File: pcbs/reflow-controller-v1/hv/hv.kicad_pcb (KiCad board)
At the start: 2 copper layers, 53 parts, among them J101 EB163A-03-C-180, J102 EB163A-02-C-180, J103 EB163A-02-C-180, J104 EB163A-02-C-180, J105 EB163A-02-C-180, J801 Power, J802 Data, Q701 MMBT3904, Q702 140357145200, U301 MOC3043SM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

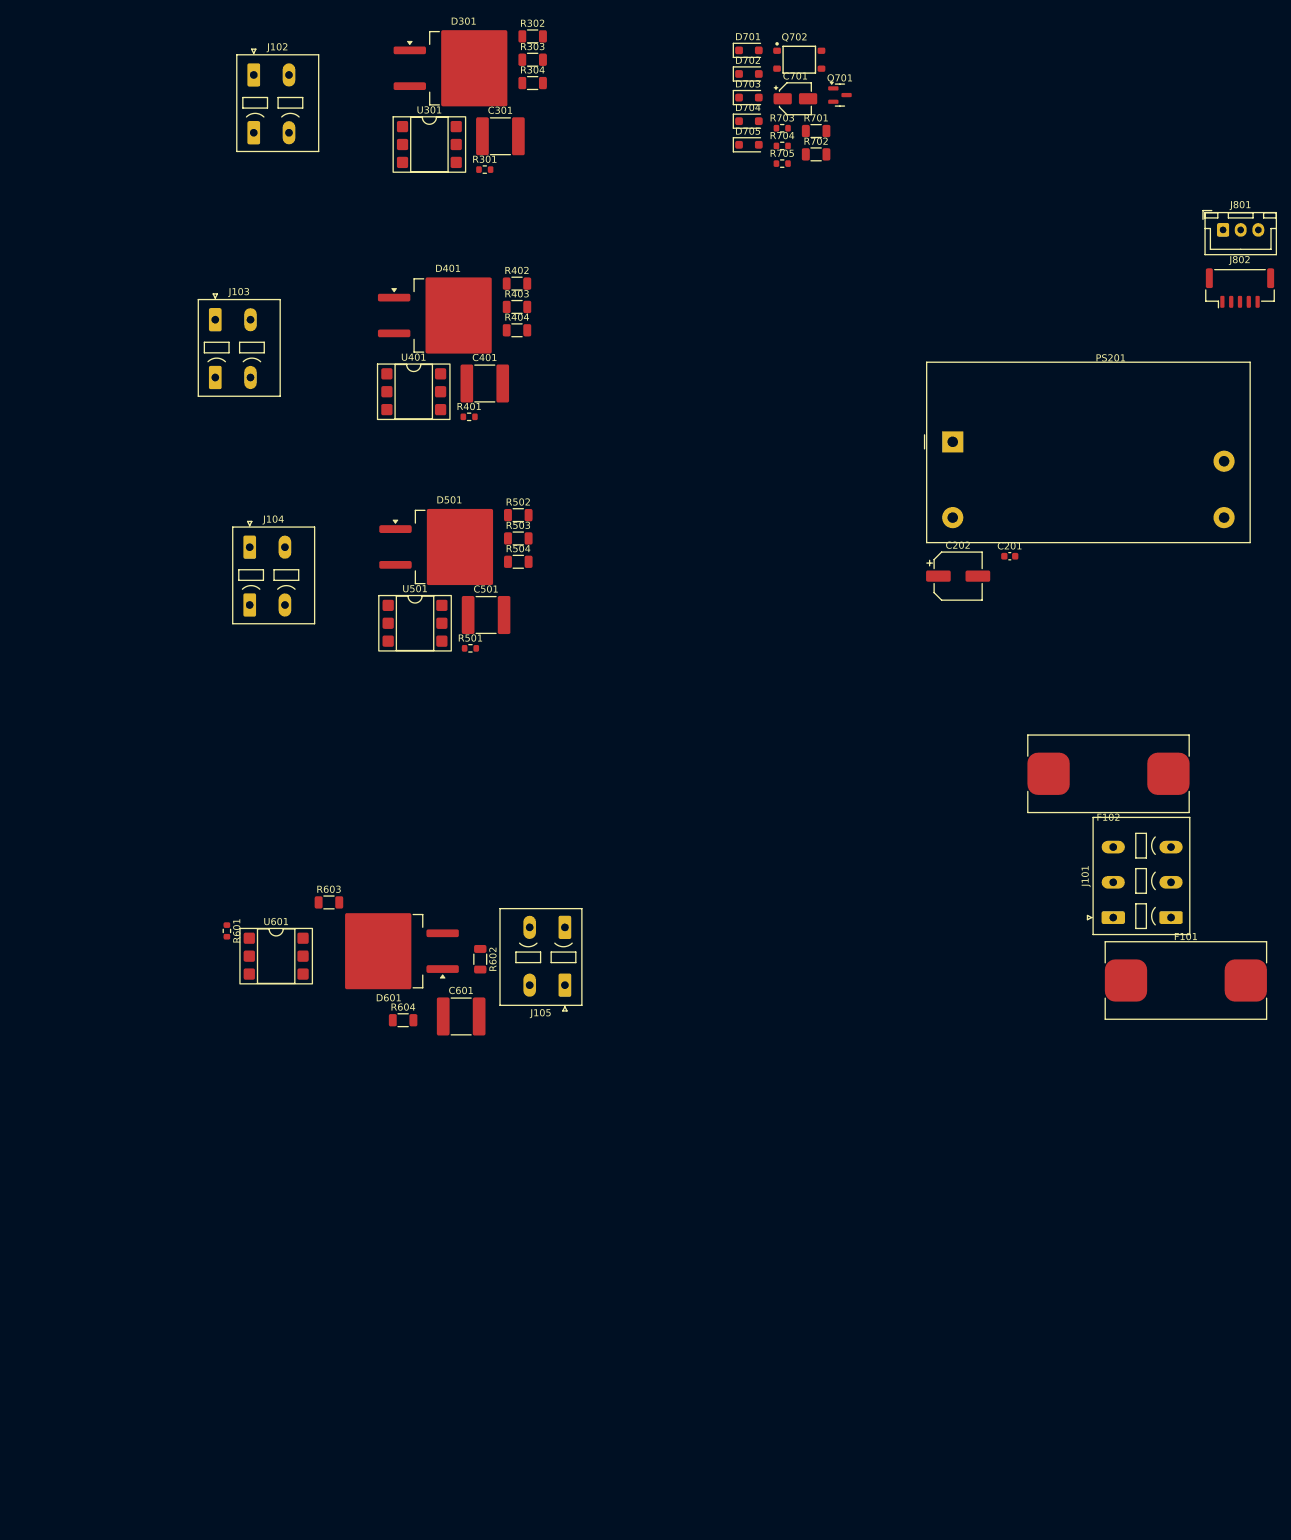
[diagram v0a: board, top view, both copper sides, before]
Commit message: Initial hv placing
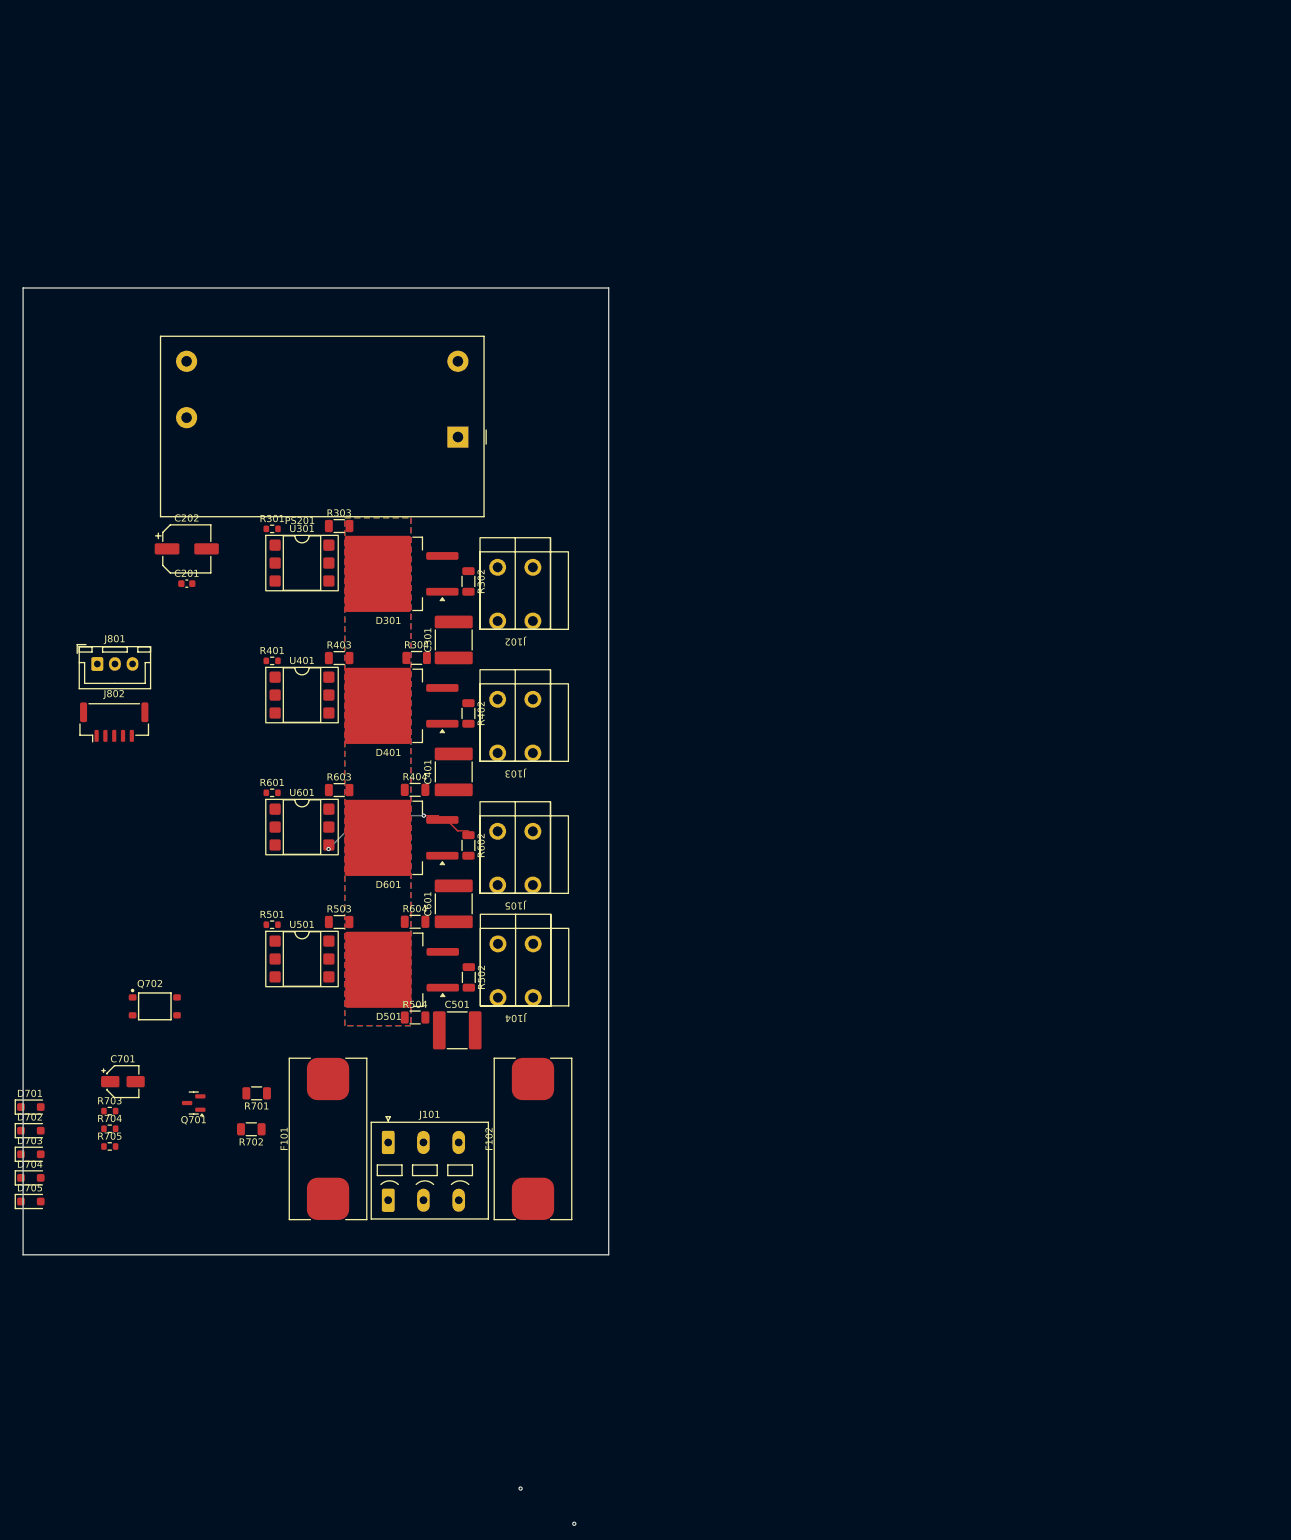
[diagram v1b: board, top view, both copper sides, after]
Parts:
- J102, J103, J104, J105: value EB163A-02-C-180 -> 691401700002B; footprint Connector_Phoenix_SPT:PhoenixContact_SPT_2.5_2-V-5.0-EX_1x02_P5.0mm_Vertical -> wuerth:691401700002B
- moved D701 181.3 mm to (41.5, 172.2)
- moved D702 181.3 mm to (41.5, 175.6)
- moved D703 181.3 mm to (41.5, 178.9)
- moved D704 181.3 mm to (41.5, 182.3)
- moved D705 181.3 mm to (41.5, 185.6)
- moved J801 171.2 mm to (51.0, 109.3)
- moved J802 171.2 mm to (53.4, 117.6)
- moved Q701 169.9 mm to (64.7, 171.7), turned to 180 degrees
- moved C701 169.0 mm to (54.6, 168.6)
- moved R703 169.0 mm to (52.7, 172.8)
- moved R704 169.0 mm to (52.7, 175.3)
- moved R705 169.0 mm to (52.7, 177.8)
- moved Q702 162.5 mm to (59.1, 157.9)
- moved R702 159.9 mm to (72.8, 175.4), turned to 180 degrees
- moved R701 157.9 mm to (73.6, 170.3), turned to 180 degrees
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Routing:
- net Net-(D601-G): track 0.00 -> 23.9 mm, vias 0 -> 2
- net (no net): vias 0 -> 2
- added copper zone on B.Cu, net /Phase_L
- added copper zone on F.Cu, net /Phase_L
- added copper zone on In1.Cu, net /Phase_L
- added copper zone on In2.Cu, net /Phase_L
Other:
- board outline added: 83.1 x 137.2 mm
- copper layers 2 -> 4

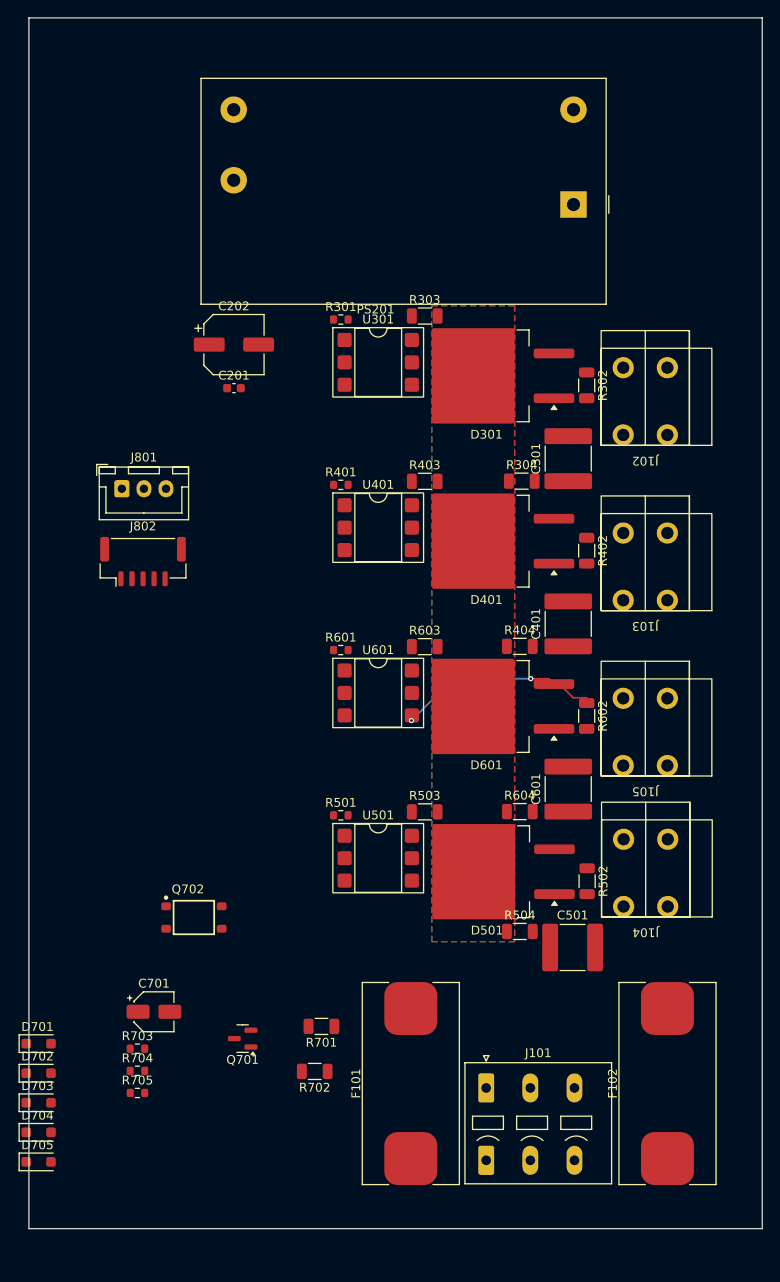
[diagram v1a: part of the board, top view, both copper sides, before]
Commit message: route hv pcb
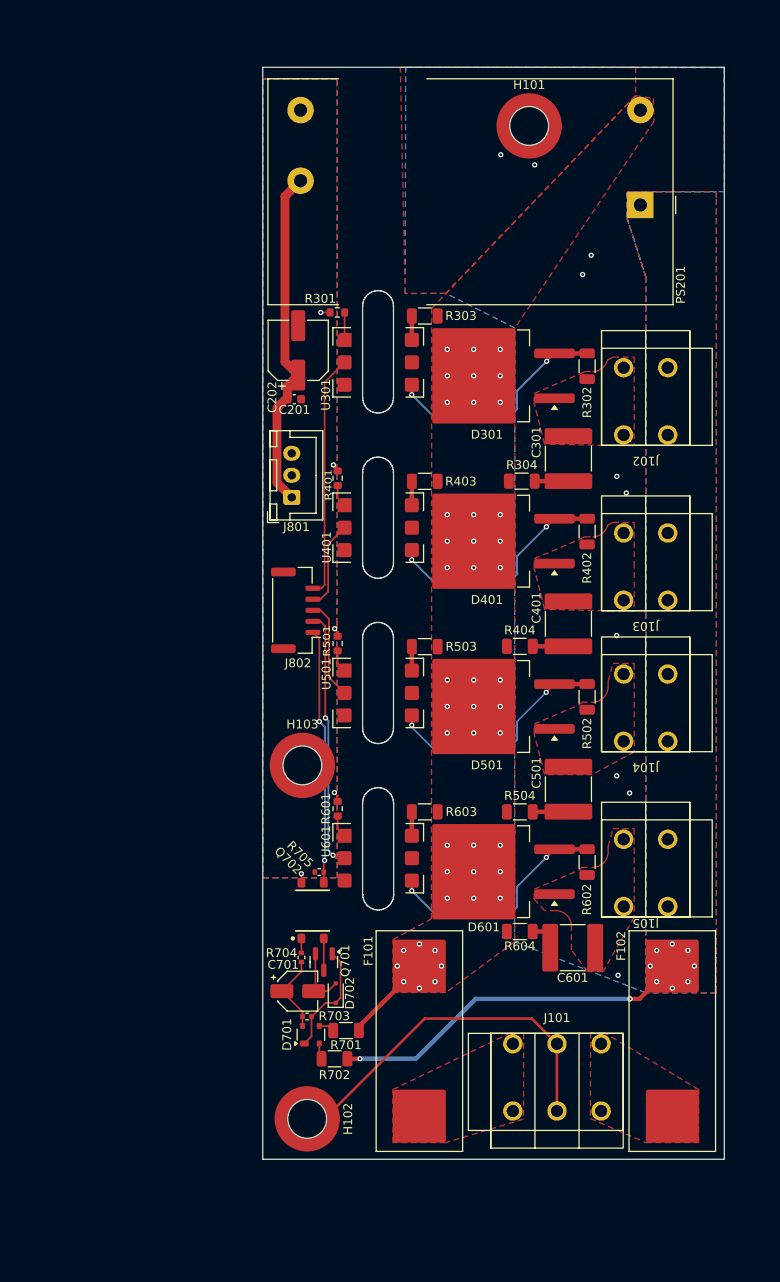
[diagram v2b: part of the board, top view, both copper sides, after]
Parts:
- removed D703, D704, D705: SL1K, Diode_SMD:D_SOD-123F
- added H101: MountingHole_Pad, Mounting_Wuerth:Mounting_Wuerth_WA-SMSR-3.2mm_H5.1mm_ReverseMount_9775051960, F.Cu at (97.1, 68.2)
- added H102: MountingHole_Pad, Mounting_Wuerth:Mounting_Wuerth_WA-SMSR-3.2mm_H5.1mm_ReverseMount_9775051960, F.Cu at (72.0, 180.7)
- added H103: MountingHole_Pad, Mounting_Wuerth:Mounting_Wuerth_WA-SMSR-3.2mm_H5.1mm_ReverseMount_9775051960, F.Cu at (71.4, 140.7)
- C202: value EEEFK1E470P -> 47μF
- D701: value SL1K -> BAS3007A-RPP; footprint Diode_SMD:D_SOD-123F -> Package_TO_SOT_SMD:SOT-143
- D702: value SL1K -> BAS21J; footprint Diode_SMD:D_SOD-123F -> Diode_SMD:D_SOD-323F
- F101, F102: value Schurter 0031.8221 -> Würth 696103101002; footprint Fuse:Fuseholder_Cylinder-5x20mm_Schurter_OGN-SMD_Horizontal_Open -> Fuse:Fuseholder_Cylinder-5x20mm_Wuerth_696103101002-SMD_Horizontal_Open
- J101: value EB163A-03-C-180 -> 691401700003B; footprint Connector_Phoenix_SPT:PhoenixContact_SPT_2.5_3-V-5.0-EX_1x03_P5.0mm_Vertical -> wuerth:691401700003B
- R301, R401, R501, R601: value 180 -> 180Ω
- R302, R402, R502, R602: value 330 -> 330Ω
- R303, R403, R503, R603: value 360 -> 360Ω
- R703, R704, R705: footprint Resistor_SMD:R_0603_1608Metric -> Resistor_SMD:R_0402_1005Metric
- moved D702 34.9 mm to (75.2, 166.5), turned to 90 degrees
- moved R705 32.4 mm to (73.4, 152.8), turned to 180 degrees
- moved D701 30.9 mm to (72.4, 171.2), turned to 90 degrees
- moved R704 22.6 mm to (71.3, 162.5), turned to -90 degrees
- moved R502 20.9 mm to (103.7, 132.9)
- moved R703 19.6 mm to (72.0, 169.1)
- moved R501 19.5 mm to (75.4, 126.9), turned to -90 degrees
- moved J801 19.3 mm to (70.2, 110.3), turned to 90 degrees
- moved D601 18.7 mm to (92.3, 152.7)
- moved R503 18.7 mm to (85.3, 127.2)
- moved R603 18.7 mm to (85.3, 146.0)
- moved D501 18.7 mm to (92.3, 134.0)
- moved J104 18.7 mm to (110.3, 132.6)
- moved U501 18.7 mm to (80.0, 132.5)
- moved U601 18.7 mm to (80.0, 151.2)
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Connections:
- C701 pad 1: Net-(D701-K) -> Net-(D701-+)
- C701 pad 2: Net-(D705-A) -> Net-(D702-A)
- D701 pad 1: Net-(D701-K) -> Net-(D701--)
- D701 pad 2: Net-(D701-A) -> Net-(D701-Pad2)
- D702 pad 1: Net-(D701-K) -> Net-(D701--)
- J801 pad 2: +3.3V -> +3V3
- J802 pad 1: /PCB Interconnect/SSR1 -> /PCB Interconnect/Zero
- J802 pad 2: /PCB Interconnect/SSR2 -> /PCB Interconnect/SSR4
- J802 pad 4: /PCB Interconnect/SSR4 -> /PCB Interconnect/SSR2
- J802 pad 5: /PCB Interconnect/Zero -> /PCB Interconnect/SSR1
- Q701 pad 1: Net-(D703-A) -> Net-(D701--)
- Q701 pad 2: Net-(D705-A) -> Net-(D702-A)
- R701 pad 2: Net-(D701-A) -> Net-(D701-Pad3)
- R702 pad 2: Net-(D702-A) -> Net-(D701-Pad2)
- R703 pad 1: Net-(D701-K) -> Net-(D701-+)
- R703 pad 2: Net-(D703-A) -> Net-(D701--)
- R704 pad 2: Net-(D701-K) -> Net-(D701-+)
- U501 pad 2: /PCB Interconnect/SSR4 -> /PCB Interconnect/SSR3
- U601 pad 2: /PCB Interconnect/SSR3 -> /PCB Interconnect/SSR4
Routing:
- net Earth_Protective: track 0.00 -> 50.1 mm, vias 0 -> 10
- net /Phase_N: track 0.00 -> 42.2 mm, vias 0 -> 10
- net +5V: track 0.00 -> 38.9 mm
- net /PCB Interconnect/SSR4: track 0.00 -> 29.4 mm, vias 0 -> 2
- net /PCB Interconnect/Zero: track 0.00 -> 29.0 mm, vias 0 -> 2
- net /PCB Interconnect/SSR1: track 0.00 -> 27.6 mm
- net Net-(D501-G): track 0.00 -> 26.6 mm, vias 0 -> 2
- net Net-(D401-G): track 0.00 -> 26.4 mm, vias 0 -> 2
- net Net-(D301-G): track 0.00 -> 26.4 mm, vias 0 -> 2
- net Net-(D701--): track 0.00 -> 13.0 mm
- net /PCB Interconnect/SSR3: track 0.00 -> 11.3 mm
- net /Phase_L: track 0.00 -> 10.1 mm, vias 0 -> 44
- net /PCB Interconnect/SSR2: track 0.00 -> 10.1 mm
- net Net-(D701-+): track 0.00 -> 9.12 mm
- net Net-(D702-A): track 0.00 -> 7.18 mm
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- added copper zone on In2.Cu, net +3V3
- added copper zone on B.Cu, net /Phase_N
- added copper zone on F.Cu, net /Phase_N
- added copper zone on In1.Cu, net /Phase_N
- added copper zone on In2.Cu, net /Phase_N
- added copper zone on F.Cu, net /Prefuse_L
- added copper zone on F.Cu, net /Prefuse_N
- added copper zone on F.Cu, net /SSR 1/MAIN_OUT
- added copper zone on F.Cu, net /SSR 2/MAIN_OUT
- added copper zone on F.Cu, net /SSR 3/MAIN_OUT
- added copper zone on F.Cu, net /SSR 4/MAIN_OUT
- added copper zone on B.Cu, net Earth_Protective
- added copper zone on F.Cu, net Earth_Protective
- added copper zone on In1.Cu, net Earth_Protective
- added copper zone on In2.Cu, net Earth_Protective
- added copper zone on B.Cu, net GND
- added copper zone on F.Cu, net GND
- added copper zone on In1.Cu, net GND
- removed copper zone on B.Cu, net /Phase_L
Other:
- board size 83.1 x 137.2 mm -> 52.3 x 123.7 mm
